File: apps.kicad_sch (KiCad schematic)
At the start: 54 parts, among them J1 Conn_01x08, J2 SWD, J3 UART, J4 Conn_01x04, Q1 AO3400A, SW1 SW_Push, SW2 SW_Push, U1 STM32F103C8Tx, U2 MCP2551, U3 AMS1117-5.0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

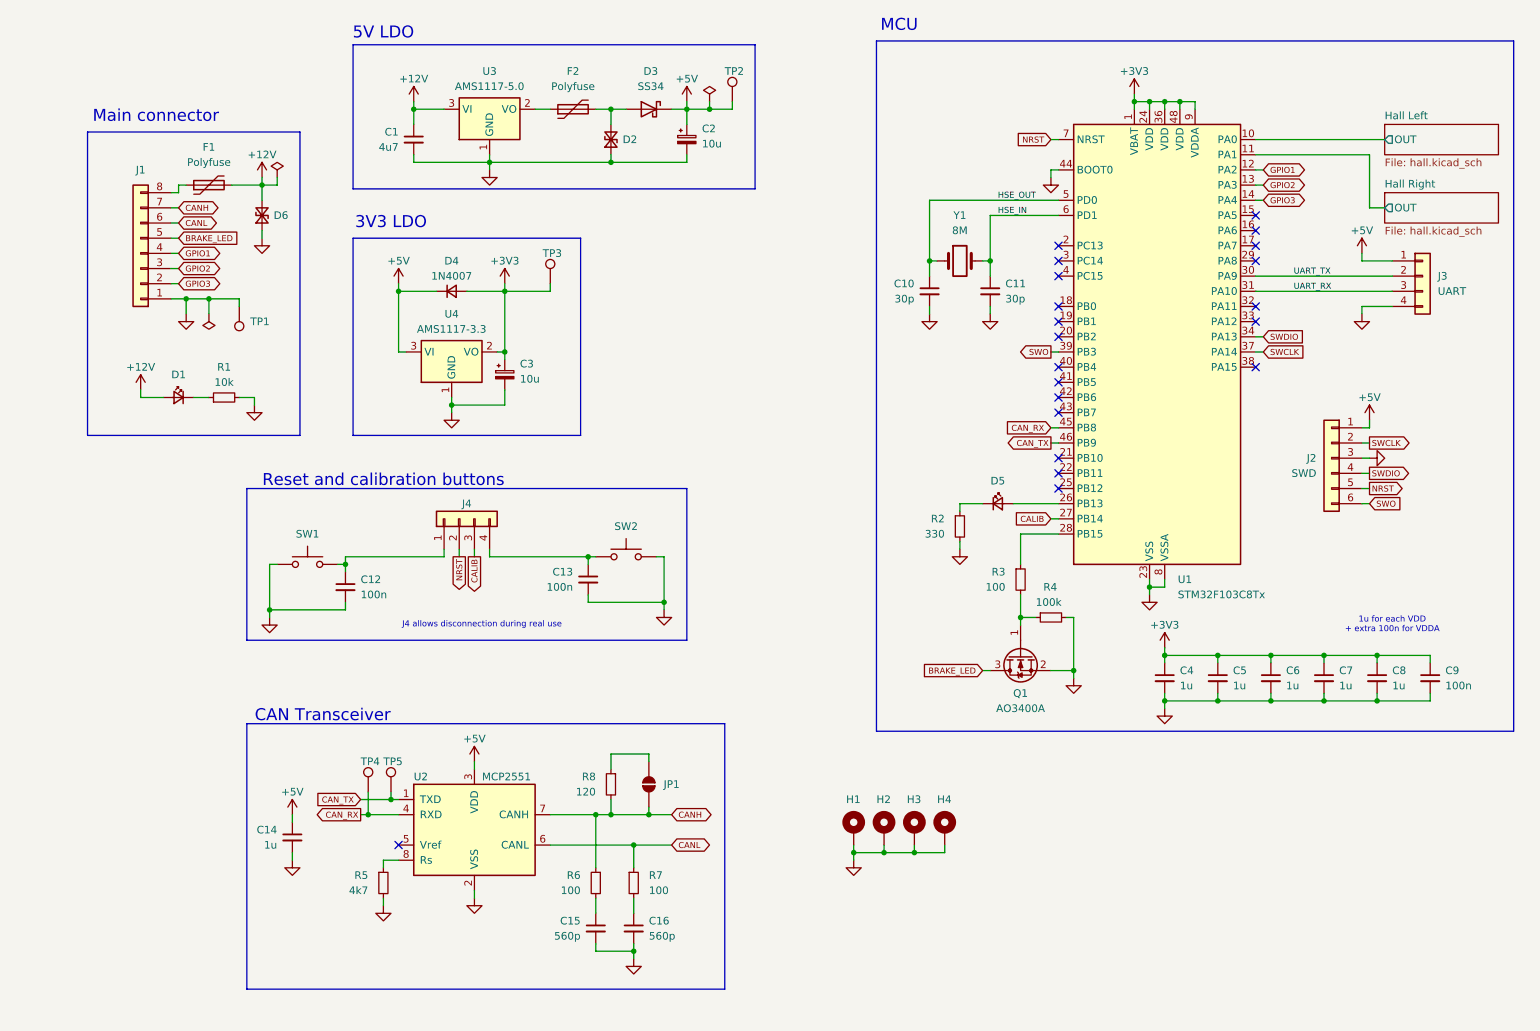
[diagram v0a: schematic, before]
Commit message: schematic: Some changes
* Add test points for hall sensors
* Assign 2.54 mm header footprints
* Fix CAN termination resistor
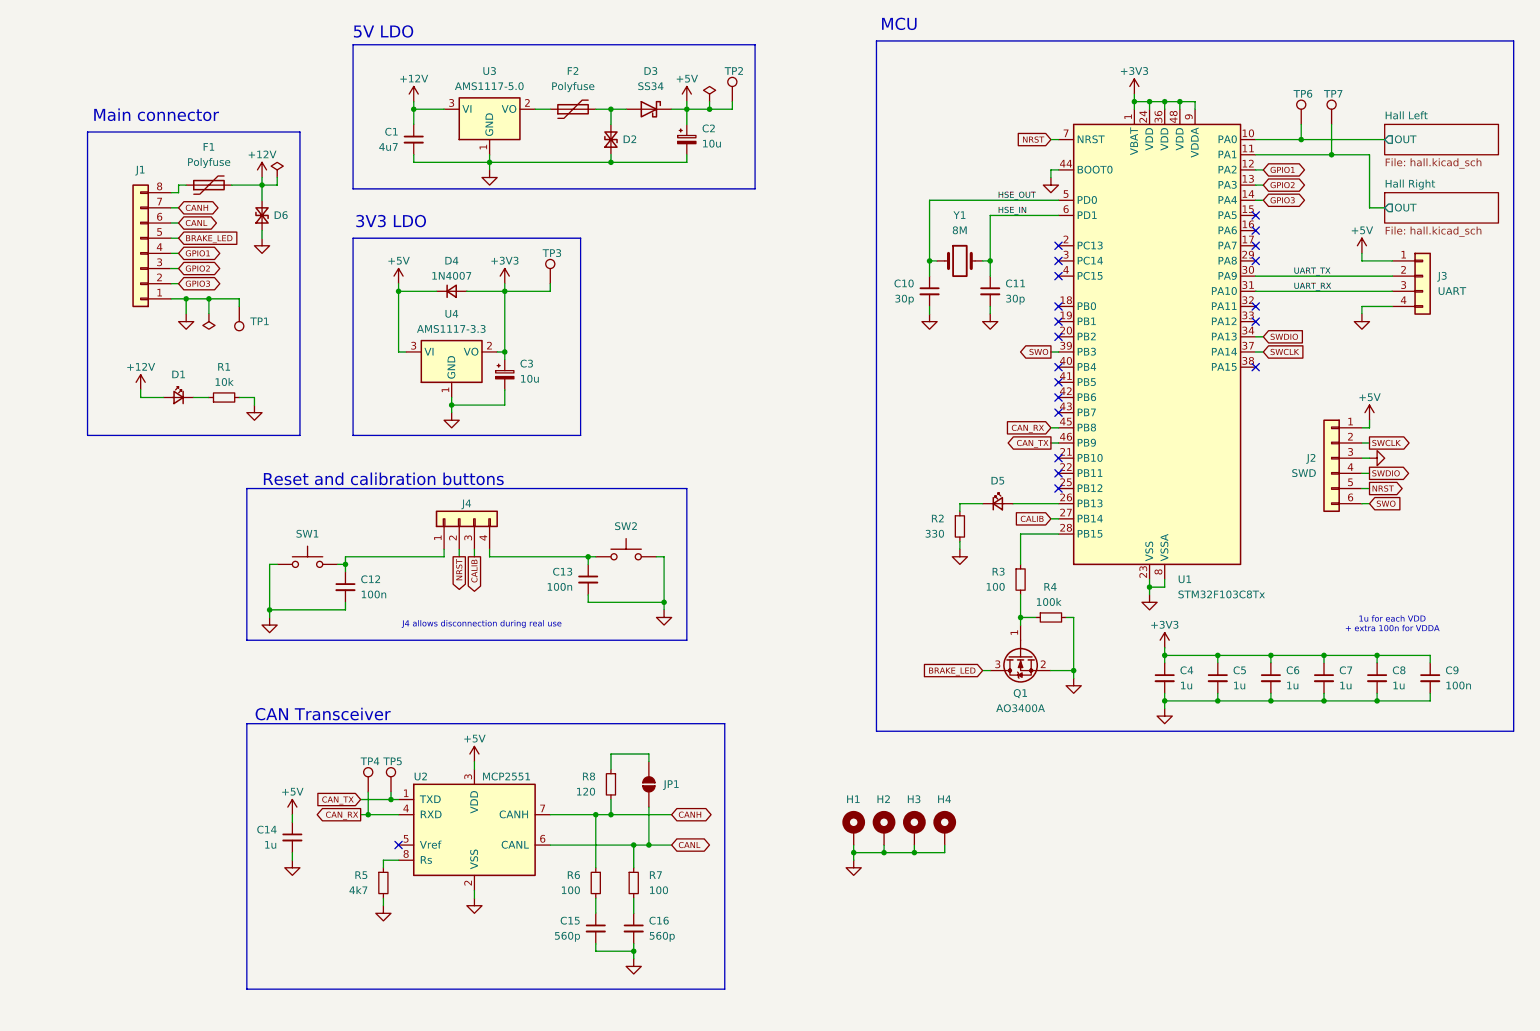
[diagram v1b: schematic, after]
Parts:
- added TP6, TP7: TestPoint, TestPoint:TestPoint_Keystone_5000-5004_Miniature, symbol Connector:TestPoint
- F1, F2: footprint (none) -> Resistor_SMD:R_0805_2012Metric
- J2: footprint (none) -> Connector_PinHeader_2.54mm:PinHeader_1x06_P2.54mm_Vertical
- J3, J4: footprint (none) -> Connector_PinHeader_2.54mm:PinHeader_1x04_P2.54mm_Vertical
- JP1: footprint (none) -> Jumper:SolderJumper-2_P1.3mm_Open_RoundedPad1.0x1.5mm
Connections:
- net CANH: no longer JP1.2 (B)
- net CANL: now also JP1.2 (B)
- net Hall Left/OUT: now also TP6.1
- net Hall Right/OUT: now also TP7.1
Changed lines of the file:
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@@
 	)
 	(junction
+		(at 227.33 41.91)
+		(diameter 0)
+		(color 0 0 0 0)
+	)
+	(junction
+		(at 118.11 160.02)
+		(diameter 0)
+		(color 0 0 0 0)
+	)
+	(junction
+		(at 232.41 44.45)
+		(diameter 0)
+		(color 0 0 0 0)
+	)
+	(junction
 		(at 231.14 128.27)
 		(diameter 0)
@@
 	)
 	(junction
-		(at 118.11 154.94)
-		(diameter 0)
-		(color 0 0 0 0)
-	)
-	(junction
 		(at 124.46 36.83)
 		(diameter 0)
@@
 	(wire
 		(pts
+			(xy 227.33 41.91) (xy 241.3 41.91)
+		)
+		(stroke
+			(width 0)
+			(type default)
+		)
+	)
+	(wire
+		(pts
 			(xy 86.36 110.49) (xy 86.36 111.76)
 		)
@@
 	(wire
 		(pts
-			(xy 219.71 44.45) (xy 238.76 44.45)
+			(xy 219.71 44.45) (xy 232.41 44.45)
 		)
 		(stroke
@@
 	(wire
 		(pts
+			(xy 118.11 160.02) (xy 121.92 160.02)
+		)
+		(stroke
+			(width 0)
+			(type default)
+		)
+	)
+	(wire
+		(pts
 			(xy 237.49 90.17) (xy 238.76 90.17)
 		)
@@
 	(wire
 		(pts
+			(xy 227.33 39.37) (xy 227.33 41.91)
+		)
+		(stroke
+			(width 0)
+			(type default)
+		)
+	)
+	(wire
+		(pts
 			(xy 111.76 44.45) (xy 111.76 45.72)
 		)
@@
 	(wire
 		(pts
-			(xy 118.11 153.67) (xy 118.11 154.94)
+			(xy 232.41 39.37) (xy 232.41 44.45)
 		)
 		(stroke
@@
 	(wire
 		(pts
-			(xy 118.11 154.94) (xy 121.92 154.94)
+			(xy 111.76 154.94) (xy 121.92 154.94)
 		)
 		(stroke
@@
 	(wire
 		(pts
+			(xy 118.11 153.67) (xy 118.11 160.02)
+		)
+		(stroke
+			(width 0)
+			(type default)
+		)
+	)
+	(wire
+		(pts
 			(xy 186.69 107.95) (xy 180.34 107.95)
 		)
@@
 	(wire
 		(pts
-			(xy 115.57 160.02) (xy 121.92 160.02)
+			(xy 115.57 160.02) (xy 118.11 160.02)
 		)
 		(stroke
@@
 	(wire
 		(pts
-			(xy 219.71 41.91) (xy 241.3 41.91)
+			(xy 219.71 41.91) (xy 227.33 41.91)
 		)
 		(stroke
@@
 	(wire
 		(pts
-			(xy 111.76 154.94) (xy 118.11 154.94)
-		)
-		(stroke
-			(width 0)
-			(type default)
-		)
-	)
-	(wire
-		(pts
 			(xy 209.55 35.56) (xy 207.01 35.56)
 		)
@@
 	(wire
 		(pts
+			(xy 232.41 44.45) (xy 238.76 44.45)
+		)
+		(stroke
+			(width 0)
+			(type default)
+		)
+	)
+	(wire
+		(pts
 			(xy 207.01 35.56) (xy 204.47 35.56)
 		)
@@
 			)
 		)
-		(property "Footprint" ""
+		(property "Footprint" "Resistor_SMD:R_0805_2012Metric"
 			(at 110.49 35.56 0)
 			(effects
@@
 	)
 	(symbol
+		(lib_id "Connector:TestPoint")
+		(at 227.33 39.37 0)
+		(unit 1)
+		(exclude_from_sim no)
+		(in_bom yes)
+		(on_board yes)
+		(dnp no)
+		(property "Reference" "TP6"
+			(at 226.06 34.29 0)
+			(effects
+				(font
+					(size 1.27 1.27)
+				)
+				(justify left)
+			)
+		)
+		(property "Value" "TestPoint"
+			(at 229.87 37.3379 0)
+			(effects
+				(font
+					(size 1.27 1.27)
+				)
+				(justify left)
+				(hide yes)
+			)
+		)
+		(property "Footprint" "TestPoint:TestPoint_Keystone_5000-5004_Miniature"
+			(at 232.41 39.37 0)
+			(effects
+				(font
+					(size 1.27 1.27)
+				)
+				(hide yes)
+			)
+		)
+		(property "Datasheet" "~"
+			(at 232.41 39.37 0)
+			(effects
+				(font
+					(size 1.27 1.27)
+				)
+				(hide yes)
+			)
+		)
+		(property "Description" "test point"
+			(at 227.33 39.37 0)
+			(effects
+				(font
+					(size 1.27 1.27)
+				)
+				(hide yes)
+			)
+		)
+		(pin "1"
+		)
+		(instances
+			(project "apps"
+				(path "/37c0128e-0bf6-47e1-84ea-e330ce83485d"
+					(reference "TP6")
+					(unit 1)
+				)
+			)
+		)
+	)
+	(symbol
 		(lib_id "Regulator_Linear:AMS1117-5.0")
 		(at 91.44 36.83 0)
@@
 			)
 		)
-		(property "Footprint" ""
+		(property "Footprint" "Connector_PinHeader_2.54mm:PinHeader_1x06_P2.54mm_Vertical"
 			(at 232.41 95.25 0)
 			(effects
@@
 			)
 		)
-		(property "Footprint" ""
+		(property "Footprint" "Connector_PinHeader_2.54mm:PinHeader_1x04_P2.54mm_Vertical"
 			(at 247.65 64.77 0)
 			(effects
@@
 	)
 	(symbol
+		(lib_id "Connector:TestPoint")
+		(at 232.41 39.37 0)
+		(unit 1)
+		(exclude_from_sim no)
+		(in_bom yes)
+		(on_board yes)
+		(dnp no)
+		(property "Reference" "TP7"
+			(at 231.14 34.29 0)
+			(effects
+				(font
+					(size 1.27 1.27)
+				)
+				(justify left)
+			)
+		)
+		(property "Value" "TestPoint"
+			(at 234.95 37.3379 0)
+			(effects
+				(font
+					(size 1.27 1.27)
+				)
+				(justify left)
+				(hide yes)
+			)
+		)
+		(property "Footprint" "TestPoint:TestPoint_Keystone_5000-5004_Miniature"
+			(at 237.49 39.37 0)
+			(effects
+				(font
+					(size 1.27 1.27)
+				)
+				(hide yes)
+			)
+		)
+		(property "Datasheet" "~"
+			(at 237.49 39.37 0)
+			(effects
+				(font
+					(size 1.27 1.27)
+				)
+				(hide yes)
+			)
+		)
+		(property "Description" "test point"
+			(at 232.41 39.37 0)
+			(effects
+				(font
+					(size 1.27 1.27)
+				)
+				(hide yes)
+			)
+		)
+		(pin "1"
+		)
+		(instances
+			(project "apps"
+				(path "/37c0128e-0bf6-47e1-84ea-e330ce83485d"
+					(reference "TP7")
+					(unit 1)
+				)
+			)
+		)
+	)
+	(symbol
 		(lib_id "MCU_ST_STM32F1:STM32F103C8Tx")
 		(at 201.93 77.47 0)
@@
 			)
 		)
-		(property "Footprint" ""
+		(property "Footprint" "Resistor_SMD:R_0805_2012Metric"
 			(at 49.53 48.26 0)
 			(effects
@@
 			)
 		)
-		(property "Footprint" ""
+		(property "Footprint" "Jumper:SolderJumper-2_P1.3mm_Open_RoundedPad1.0x1.5mm"
 			(at 118.11 149.86 0)
 			(effects
@@
 			)
 		)
-		(property "Footprint" ""
+		(property "Footprint" "Connector_PinHeader_2.54mm:PinHeader_1x04_P2.54mm_Vertical"
 			(at 86.36 105.41 0)
 			(effects

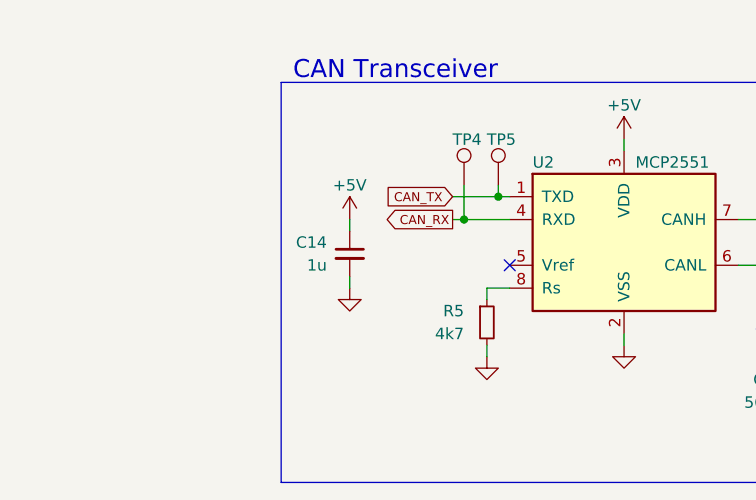
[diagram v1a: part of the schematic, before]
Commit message: schematic: Add ESD TVS diodes for CAN bus
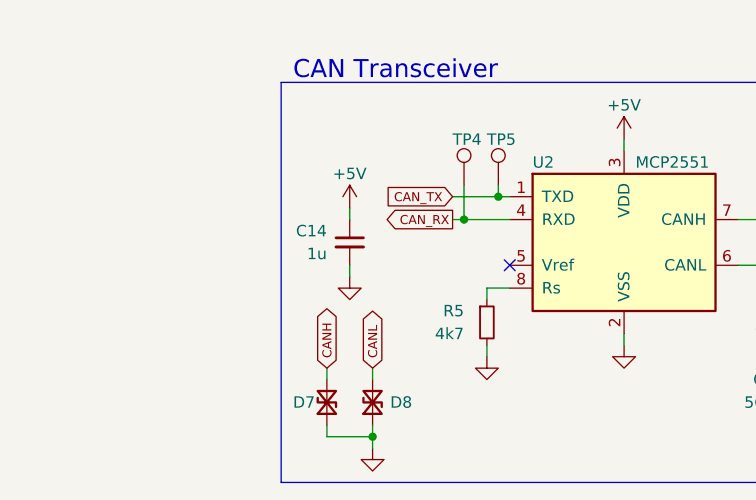
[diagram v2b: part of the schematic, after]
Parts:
- added D7, D8: H5VL10B, symbol Device:D_TVS_Small
- D2: value D_TVS_Small -> H5VL10B
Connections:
- net CANH: now also D7.2 (A2)
- net CANL: now also D8.2 (A2)
- net GND: now also D7.1 (A1), D8.1 (A1)
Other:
- moved on the sheet: C14

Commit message: schematic: Assign footprints for 12 V diodes
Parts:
- D6: value D_TVS_Small -> UDD32C12L01-ES; footprint (none) -> Diode_SMD:D_SOD-323
- D7, D8: value H5VL10B -> UDD32C12L01-ES; footprint (none) -> Diode_SMD:D_SOD-323
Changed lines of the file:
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@@
 			)
 		)
-		(property "Value" "D_TVS_Small"
+		(property "Value" "UDD32C12L01-ES"
 			(at 49.53 54.61 0)
 			(effects
@@
 			)
 		)
-		(property "Footprint" ""
+		(property "Footprint" "Diode_SMD:D_SOD-323"
 			(at 53.34 54.61 0)
 			(effects
@@
 			)
 		)
-		(property "Value" "H5VL10B"
+		(property "Value" "UDD32C12L01-ES"
 			(at 52.07 175.26 0)
 			(effects
@@
 			)
 		)
-		(property "Footprint" ""
+		(property "Footprint" "Diode_SMD:D_SOD-323"
 			(at 55.88 175.26 0)
 			(effects
@@
 			)
 		)
-		(property "Value" "H5VL10B"
+		(property "Value" "UDD32C12L01-ES"
 			(at 57.15 175.26 0)
 			(effects
@@
 			)
 		)
-		(property "Footprint" ""
+		(property "Footprint" "Diode_SMD:D_SOD-323"
 			(at 60.96 175.26 0)
 			(effects

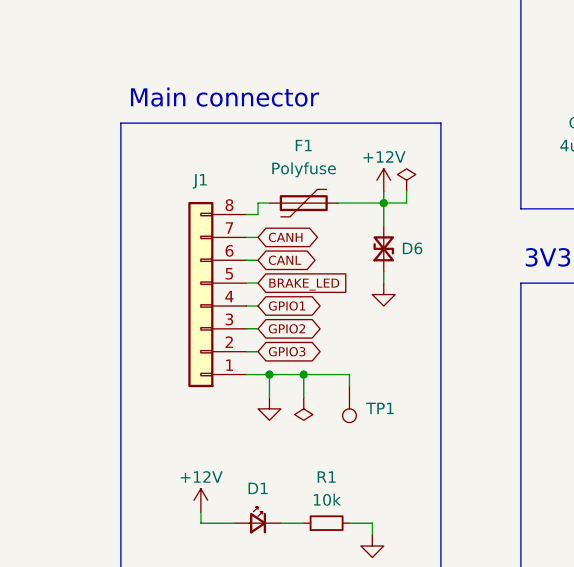
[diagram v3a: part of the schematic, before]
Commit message: schematic: Add symbol and footprint for main connector
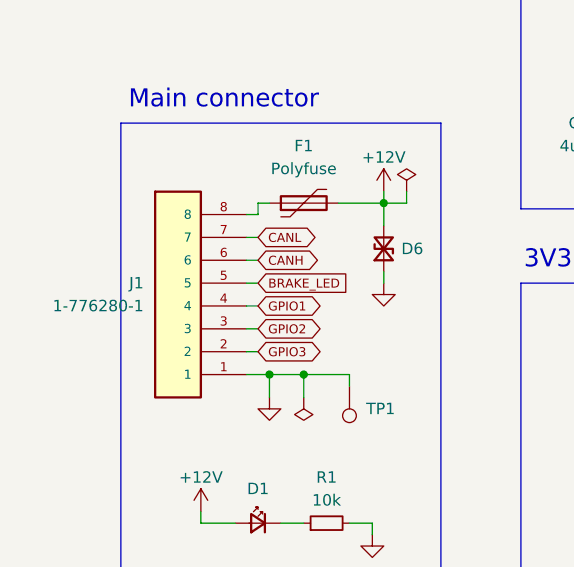
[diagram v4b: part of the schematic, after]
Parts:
- removed J1: Conn_01x08, symbol Connector_Generic:Conn_01x08
- added J1: 1-776280-1, TE_1-776280-1, symbol 1-776280-1:1-776280-1
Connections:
- net BRAKE_LED: now also J1.5
- net CANH: now also J1.6
- net CANL: now also J1.7
- net GND: now also J1.1
- net GPIO1: now also J1.4
- net GPIO2: now also J1.3
- net GPIO3: now also J1.2
- net at F1.1: now also J1.8
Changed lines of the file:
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@@
 	(label "HSE_IN"
 		(at 176.53 54.61 0)
+		(fields_autoplaced yes)
 		(effects
 			(font
@@
 	(label "HSE_OUT"
 		(at 176.53 52.07 0)
+		(fields_autoplaced yes)
 		(effects
 			(font
@@
 	(label "UART_RX"
 		(at 226.06 67.31 0)
+		(fields_autoplaced yes)
 		(effects
 			(font
@@
 	(label "UART_TX"
 		(at 226.06 64.77 0)
+		(fields_autoplaced yes)
 		(effects
 			(font
@@
 	(global_label "CANH"
 		(shape bidirectional)
-		(at 39.37 53.34 0)
+		(at 39.37 55.88 0)
 		(fields_autoplaced yes)
 		(effects
@@
 		)
 		(property "Intersheetrefs" "${INTERSHEET_REFS}"
-			(at 46.5476 53.34 0)
+			(at 46.5476 55.88 0)
 			(effects
 				(font
@@
 	(global_label "CANL"
 		(shape bidirectional)
-		(at 39.37 55.88 0)
+		(at 39.37 53.34 0)
 		(fields_autoplaced yes)
 		(effects
@@
 		)
 		(property "Intersheetrefs" "${INTERSHEET_REFS}"
-			(at 46.3095 55.88 0)
+			(at 46.3095 53.34 0)
 			(effects
 				(font
@@
 	)
 	(symbol
-		(lib_id "Connector_Generic:Conn_01x08")
-		(at 33.02 60.96 180)
-		(unit 1)
-		(exclude_from_sim no)
-		(in_bom yes)
-		(on_board yes)
-		(dnp no)
-		(fields_autoplaced yes)
-		(property "Reference" "J1"
-			(at 33.02 46.99 0)
-			(effects
-				(font
-					(size 1.27 1.27)
-				)
-			)
-		)
-		(property "Value" "Conn_01x08"
-			(at 30.48 58.4201 0)
-			(effects
-				(font
-					(size 1.27 1.27)
-				)
-				(justify left)
-				(hide yes)
-			)
-		)
-		(property "Footprint" ""
-			(at 33.02 60.96 0)
-			(effects
-				(font
-					(size 1.27 1.27)
-				)
-				(hide yes)
-			)
-		)
-		(property "Datasheet" "~"
-			(at 33.02 60.96 0)
-			(effects
-				(font
-					(size 1.27 1.27)
-				)
-				(hide yes)
-			)
-		)
-		(property "Description" "Generic connector, single row, 01x08, script generated (kicad-library-utils/schlib/autogen/connector/)"
-			(at 33.02 60.96 0)
-			(effects
-				(font
-					(size 1.27 1.27)
-				)
-				(hide yes)
-			)
-		)
-		(pin "4"
-		)
-		(pin "3"
-		)
-		(pin "2"
-		)
-		(pin "6"
-		)
-		(pin "7"
-		)
-		(pin "1"
-		)
-		(pin "5"
-		)
-		(pin "8"
-		)
-		(instances
-			(project ""
-				(path "/37c0128e-0bf6-47e1-84ea-e330ce83485d"
-					(reference "J1")
-					(unit 1)
-				)
-			)
-		)
-	)
-	(symbol
 		(lib_id "Device:LED_Small")
 		(at 176.53 102.87 0)
@@
 					(unit 1)
 				)
+			)
+		)
+	)
+	(symbol
+		(lib_id "1-776280-1:1-776280-1")
+		(at 30.48 60.96 0)
+		(mirror x)
+		(unit 1)
+		(exclude_from_sim no)
+		(in_bom yes)
+		(on_board yes)
+		(dnp no)
+		(fields_autoplaced yes)
+		(property "Reference" "J1"
+			(at 26.67 58.4199 0)
+			(effects
+				(font
+					(size 1.27 1.27)
+				)
+				(justify right)
+			)
+		)
+		(property "Value" "1-776280-1"
+			(at 26.67 60.9599 0)
+			(effects
+				(font
+					(size 1.27 1.27)
+				)
+				(justify right)
+			)
+		)
+		(property "Footprint" "TE_1-776280-1"
+			(at 30.48 60.96 0)
+			(effects
+				(font
+					(size 1.27 1.27)
+				)
+				(justify left bottom)
+				(hide yes)
+			)
+		)
+		(property "Datasheet" ""
+			(at 30.48 60.96 0)
+			(effects
+				(font
+					(size 1.27 1.27)
+				)
+				(justify left bottom)
+				(hide yes)
+			)
+		)
+		(property "Description" ""
+			(at 30.48 60.96 0)
+			(effects
+				(font
+					(size 1.27 1.27)
+				)
+				(hide yes)
+			)
+		)
+		(property "PARTREV" "F8"
+			(at 30.48 60.96 0)
+			(effects
+				(font
+					(size 1.27 1.27)
+				)
+				(justify left bottom)
+				(hide yes)
+			)
+		)
+		(property "METADATA" "Manufacturer recommendations"
+			(at 30.48 60.96 0)
+			(effects
+				(font
+					(size 1.27 1.27)
+				)
+				(justify left bottom)
+				(hide yes)
+			)
+		)
+		(property "MANUFACTURER" "TE Connectivity"
+			(at 30.48 60.96 0)
+			(effects
+				(font
+					(size 1.27 1.27)
+				)
+				(justify left bottom)
+				(hide yes)
+			)
+		)
+		(pin "3"
+		)
+		(pin "1"
+		)
+		(pin "4"
+		)
+		(pin "5"
+		)
+		(pin "6"
+		)
+		(pin "7"
+		)
+		(pin "2"
+		)
+		(pin "8"
+		)
+		(instances
+			(project ""
+				(path "/37c0128e-0bf6-47e1-84ea-e330ce83485d"
+					(reference "J1")
+					(unit 1)
+				)
